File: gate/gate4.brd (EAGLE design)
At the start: 57.1 x 82.5 mm, 32 parts, among them J1 MOLEX_MINILITE_TRAP_2, J2 MOLEX_MINILITE_TRAP_2, J3 MOLEX_MINILITE_TRAP_2, J4 MOLEX_MINILITE_TRAP_2, J8 MOLEX_MINILITE_TRAP_2, J9 MOLEX_MINILITE_TRAP_2, U1 SN75468

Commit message: Gate 4, and misc updates
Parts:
- removed J10: (no value), SparkFun-Connectors:1X07
- removed JP0, JP1: JUMPER-PAD-3-2OF3_NC_BY_TRACE_SMALL, SparkFun-Passives:PAD-JUMPER-3-2OF3_NC_BY_TRACE_YES_SILK_FULL_BOX
- added JP7, JP8: JUMPER-PAD-2-NOYES_SILK, SparkFun-Passives:PAD-JUMPER-2-NO_YES_SILK
- added SJ1: (no value), jumper:SJ
- added ST5: (no value), Puffin:SCREWTERM_0.2X2
- J5: device SparkFun-Connectors:2X4 -> SparkFun-Connectors:1X07
- J9: value MOLEX_MINILITE_TRAP_2 -> (none); device Puffin:MOLEX_MINILITE_TRAP_2 -> SparkFun-Connectors:1X04
- JP2, JP3, JP4, JP5, JP6: value JUMPER-PAD-3-2OF3_NC_BY_TRACE_SMALL -> JUMPER-PAD-2-NOYES_SILK; device SparkFun-Passives:PAD-JUMPER-3-2OF3_NC_BY_TRACE_YES_SILK_FULL_BOX -> SparkFun-Passives:PAD-JUMPER-2-NO_YES_SILK
- moved R1 66.6 mm to (41.9, 74.2)
- moved J1 63.0 mm to (52.1, 66.8)
- moved ST4 57.1 mm to (54.6, 2.54)
- moved R2 54.4 mm to (41.9, 68.3)
- moved R7 50.8 mm to (23.6, 8.89)
- moved J2 50.5 mm to (52.1, 60.7)
- moved R3 42.3 mm to (41.9, 62.5)
- moved J5 38.9 mm to (16.5, 34.3), turned to 270 degrees
- moved J3 38.1 mm to (52.1, 54.6)
- moved H1 33.1 mm to (43.2, 3.17)
- moved PS1 31.2 mm to (31.8, 47.5), turned to 90 degrees
- moved R4 30.1 mm to (41.9, 56.6)
- moved J4 27.2 mm to (43.4, 48.5)
- moved ST3 26.7 mm to (54.6, 17.8)
- moved R6 24.6 mm to (23.6, 21.6)
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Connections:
- removed net D0: E1.D0, JP0.3
- removed net D1: E1.D1, JP1.3
- removed net D2: E1.D2, JP2.3
- removed net D3: E1.D3, JP3.3
- removed net D4: E1.D4, JP4.3
- removed net D5: E1.D5, JP5.3
- removed net D6: E1.D6, JP6.3
- removed net J0: J10.1, JP0.2
- removed net J1: J10.2, JP1.2
- removed net J2: J10.3, JP2.2
- removed net J3: J10.4, JP3.2
- removed net J4: J10.5, JP4.2
- removed net J5: J10.6, JP5.2
- removed net J6: J10.7, JP6.2
- new net N$22: R2.3, U1.15
- new net N$30: E1.D0, J5.7, JP8.2
- new net N$31: E1.D1, J5.6, JP7.2
- new net N$32: E1.D2, J5.5, JP6.2
- new net N$36: E1.D4, J5.3, JP4.2
- new net N$37: E1.D5, J5.2, JP3.2
- new net N$38: E1.D6, J5.1, JP2.2
- net 3.3V: now also J9.3; no longer J5.5, J5.6
- net 5V: now also J9.2, SJ1.2; no longer J5.3, J5.4, J9.1
- net A0: now also JP8.1; no longer JP0.1
- net A1: now also JP7.1; no longer JP1.1
- net A2: now also JP6.1; no longer JP2.1
- net A3: now also JP5.1; no longer JP3.1
- net A5: now also JP3.1; no longer JP5.1
- net A6: now also JP2.1; no longer JP6.1
- net GND: now also J9.4, ST5.1; no longer J5.7, J5.8, J9.2
- net N$1: now also ST1.2; no longer ST1.1
- net N$23: now also ST1.1; no longer ST1.2
- net N$3: now also R5.1; no longer R3.3
- net N$33: now also R1.3; no longer R7.1
- net N$34: now also E1.D3, J5.4, JP5.2; no longer R6.1, U1.15
- net N$35: now also R3.3; no longer R5.1
- net N$4: now also R6.1; no longer R2.3
- net N$5: now also R7.1; no longer R1.3
- net VIN: now also J9.1, SJ1.1, ST5.2; no longer J5.1, J5.2
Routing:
- net N$23: track 49.9 -> 5.40 mm
- net N$1: track 42.5 -> 5.40 mm
- net A1: track 26.4 -> 60.4 mm, vias 1 -> 0
- net A0: track 27.9 -> 61.6 mm
- net A3: track 24.1 -> 57.8 mm, vias 1 -> 0
- net A5: track 23.7 -> 55.3 mm, vias 1 -> 0
- net A2: track 28.7 -> 59.1 mm, vias 1 -> 0
- net A4: track 27.4 -> 56.6 mm, vias 1 -> 0
- net A6: track 26.3 -> 54.0 mm, vias 1 -> 0
- net J5: track 20.5 -> 0.00 mm, vias 1 -> 0
- net J3: track 20.3 -> 0.00 mm, vias 1 -> 0
- net J1: track 20.3 -> 0.00 mm, vias 1 -> 0
- net N$22: track 0.00 -> 18.7 mm
- net J0: track 18.1 -> 0.00 mm, vias 1 -> 0
- net J4: track 17.5 -> 0.00 mm, vias 1 -> 0
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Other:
- board text added: "3V3"
- board text added: "V4"
- board text removed: "AC"

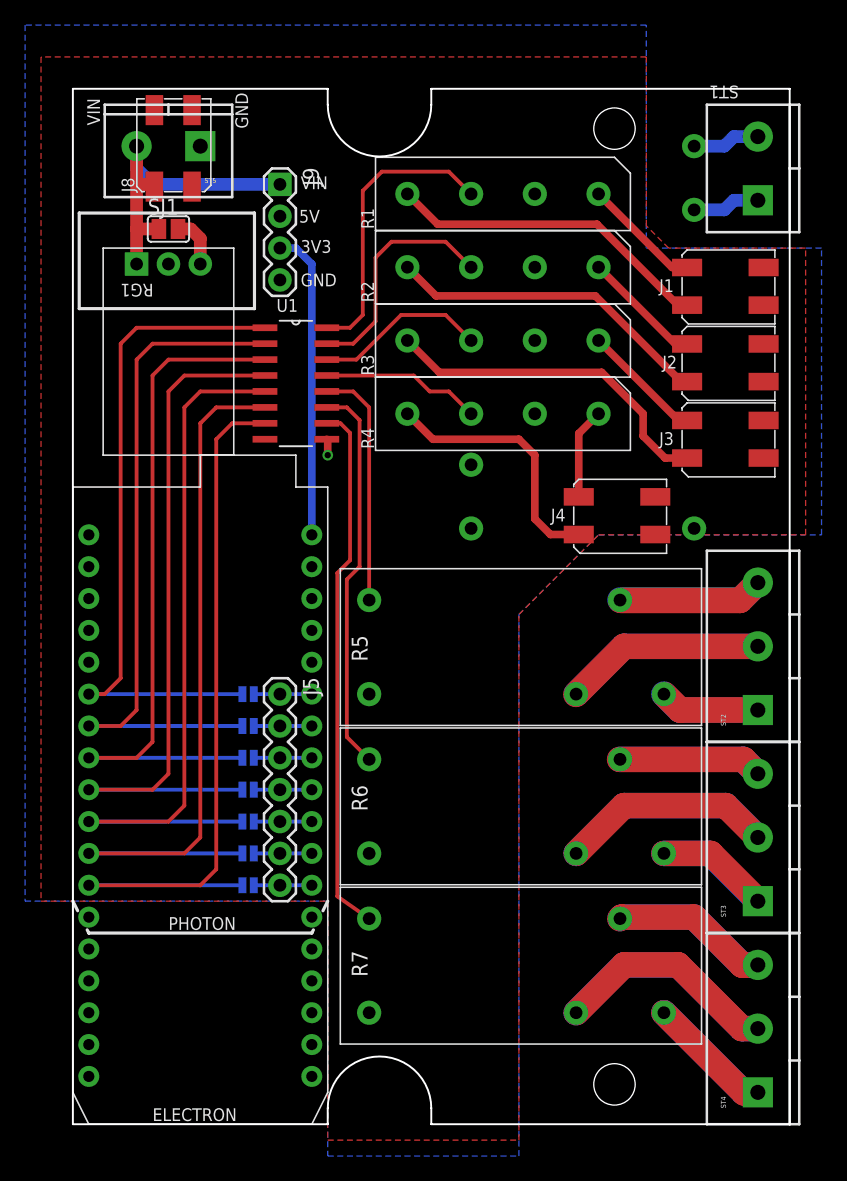
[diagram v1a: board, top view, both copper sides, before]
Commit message: Update gate4, new gate5 with eseries
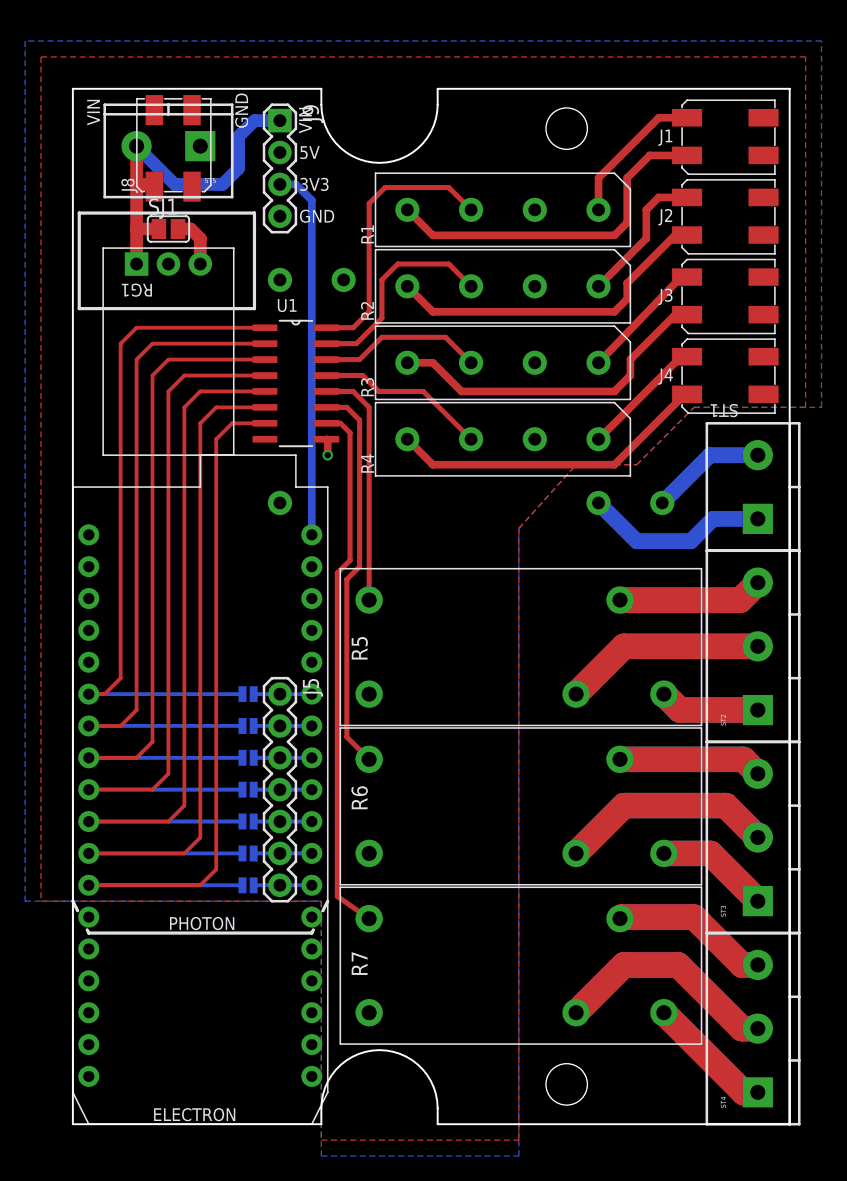
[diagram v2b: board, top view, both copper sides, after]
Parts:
- moved ST1 25.4 mm to (54.6, 48.3)
- moved PS1 25.0 mm to (16.5, 67.3), turned to 180 degrees
- moved J4 14.1 mm to (52.1, 59.7)
- moved J1 11.9 mm to (52.1, 78.7)
- moved J2 11.7 mm to (52.1, 72.4)
- moved J3 11.4 mm to (52.1, 66.0)
- moved J9 5.08 mm to (16.5, 80.0)
- moved H1 3.81 mm to (39.4, 3.17)
- moved H2 3.81 mm to (39.4, 79.4)
- moved R4 2.03 mm to (41.9, 54.6)
- moved R3 1.78 mm to (41.9, 60.7)
- moved R2 1.52 mm to (41.9, 66.8)
- moved R1 1.27 mm to (41.9, 72.9)
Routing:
- net N$23: track 5.40 -> 14.7 mm
- net 3.3V: track 24.7 -> 29.7 mm
- net N$6: track 20.6 -> 25.5 mm
- net N$1: track 5.40 -> 9.20 mm
- net VIN: track 26.4 -> 28.9 mm
- net N$11: track 7.28 -> 9.79 mm
- net N$13: track 9.49 -> 11.6 mm
- net N$22: track 18.7 -> 16.7 mm
- net N$12: track 26.0 -> 27.9 mm
- net N$9: track 9.59 -> 11.3 mm
- net N$33: track 23.2 -> 21.9 mm
- net N$2: track 12.8 -> 13.6 mm
- net N$35: track 13.8 -> 13.1 mm
- net N$7: track 27.2 -> 26.5 mm
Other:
- outline, holes or cut-outs redrawn
- board text added: "AC IN"
